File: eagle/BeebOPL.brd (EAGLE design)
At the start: 100 x 80 mm, 44 parts, among them IC1 LM324N, IC2 YM3014B, IC3 LM7805, IC5 74LS02N, IC6 YM3812, IC7 74LS04N, IC9 74HCT688N, J1 1 MHz Bus, J2 Feed-through, J3 3.5mm Jack, J4 DC-IN

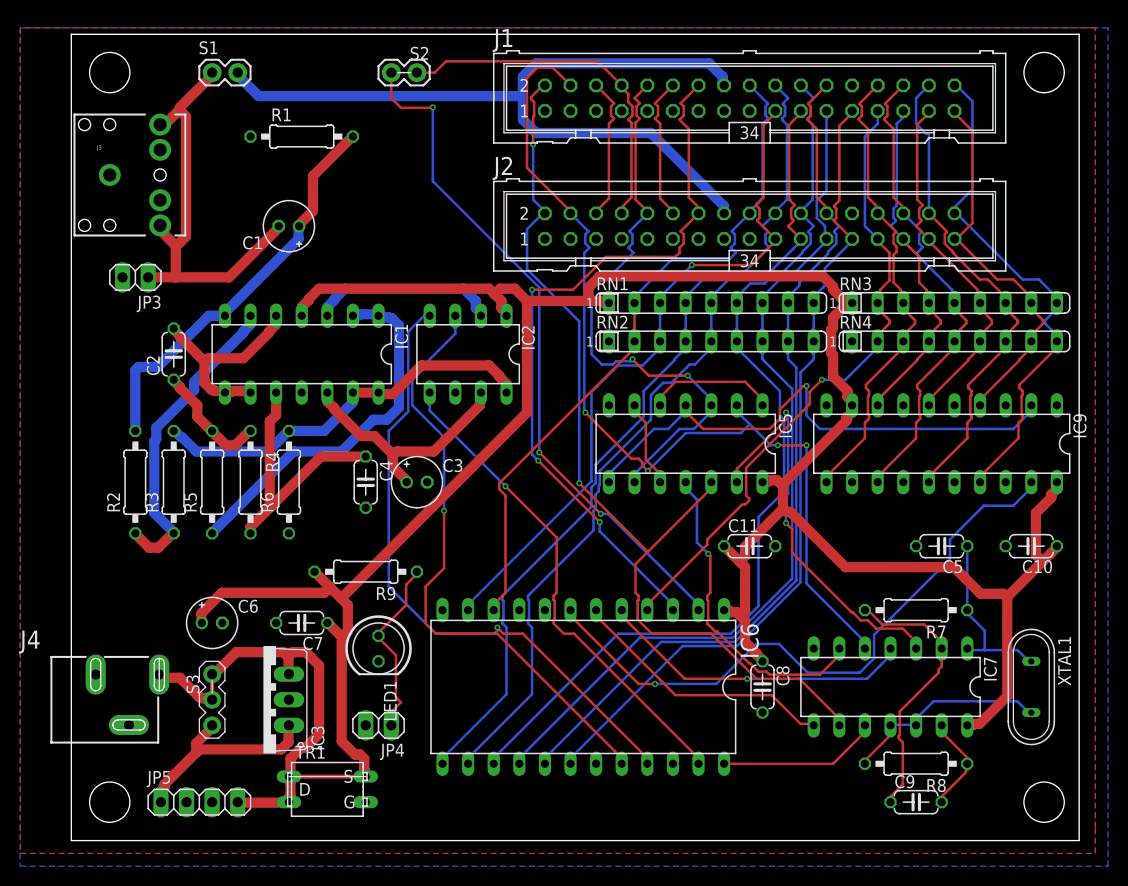
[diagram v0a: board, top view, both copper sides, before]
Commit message: Added silkscreen
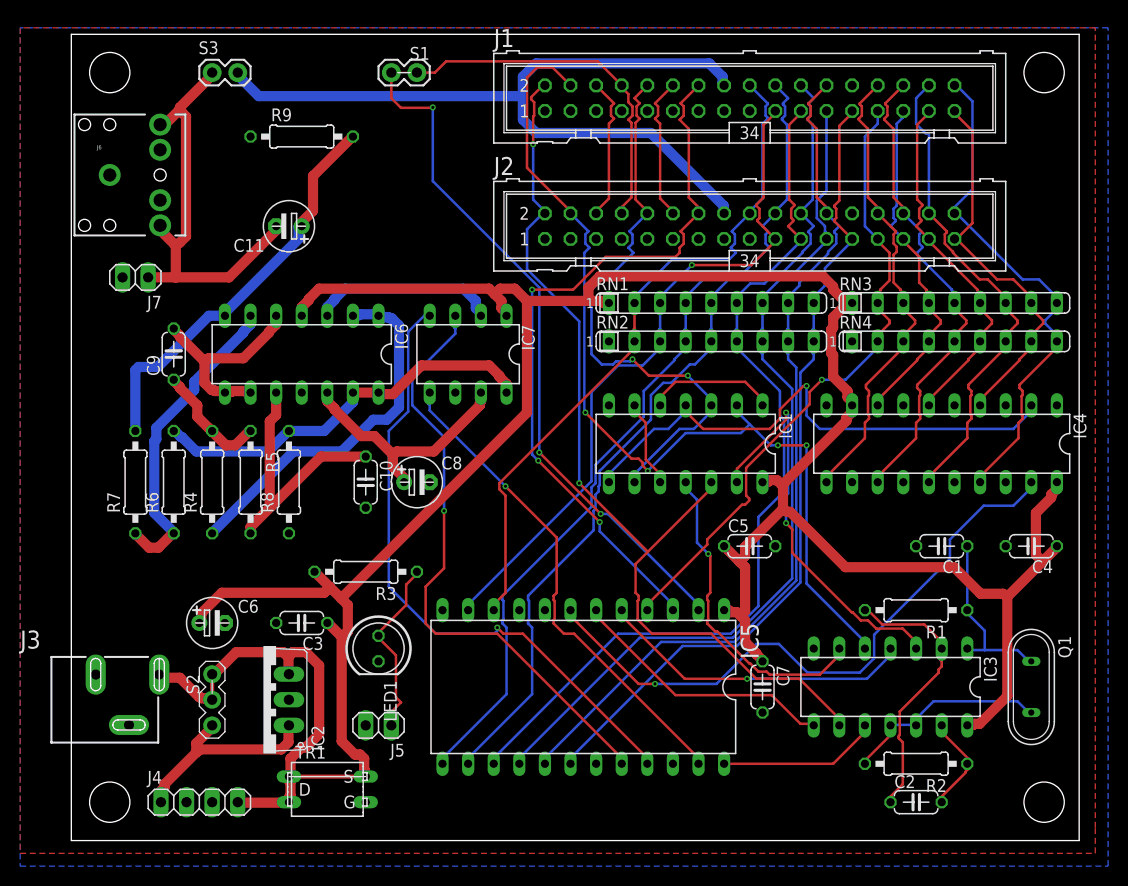
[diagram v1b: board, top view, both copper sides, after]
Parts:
- removed JP5: PWR, pinhead:1X04
- added J6: 3.5mm Jack, SparkFun-Connectors:AUDIO-JACK
- added LOGO1: OSHW-LOGO-BOTTOML, YMSynth:OSHW-LOGO-L
- C1: value 4.7uF 35V -> 82pF; device resistor:E2-5 -> resistor:C050-024X044
- C10: value 100nF -> 220pF
- C11: value 100nF -> 4.7uF 35V; device resistor:C050-024X044 -> YMSynth:E2,5-5
- C2: value 470pF -> 4.7nF
- C3: value 10uF 16V -> 10nF; device resistor:E2-5 -> resistor:C050-024X044
- C4: value 220pF -> 100nF
- C5: value 82pF -> 100nF
- C6: device resistor:E2-5 -> YMSynth:E2,5-5
- C8: value 10nF -> 10uF 16V; device resistor:C050-024X044 -> YMSynth:E2,5-5
- C9: value 4.7nF -> 470pF
- IC1: value LM324N -> 74LS02N; device linear:DIL14 -> 74xx-us:DIL14
- IC2: value YM3014B -> LM7805; device YMSynth:YM3014B -> linear:TO220V
- IC3: value LM7805 -> 74LS04N; device linear:TO220V -> 74xx-us:DIL14
- IC5: value 74LS02N -> YM3812; device 74xx-us:DIL14 -> YMSynth:YM3812
- IC6: value YM3812 -> LM324N; device YMSynth:YM3812 -> linear:DIL14
- IC7: value 74LS04N -> YM3014B; device 74xx-us:DIL14 -> YMSynth:YM3014B
- J3: value 3.5mm Jack -> DC in; device SparkFun-Connectors:AUDIO-JACK -> SparkFun-Connectors:POWER_JACK_SLOT
- J4: value DC-IN -> PWR; device SparkFun-Connectors:POWER_JACK_SLOT -> pinhead:1X04
- J7: value AUDIO -> Audio
- R1: value 4k7 -> 470R
- R2: value 27k -> 470R
- R3: value 15k -> 470R
- R6: value 4k7 -> 15k
- R7: value 470R -> 27k
- R8, R9: value 470R -> 4k7
- RN1, RN2, RN3, RN4: value 2k2 -> 2k2 x 8
- S1: value 1MHz Bus Audio -> IRQ enable; device SparkFun-Retired:1X02 -> YMSynth:1X02
- S2: value IRQ -> pwr sel; device YMSynth:1X02 -> YMSynth:S_3WAY_OR
- S3: value REG -> 1MHz Bus Audio; device YMSynth:S_3WAY_OR -> SparkFun-Retired:1X02
- moved C2 86.0 mm to (83.8, 3.81), turned to 0 degrees
- moved C9 86.0 mm to (10.2, 48.3), turned to 90 degrees
- moved R2 82.4 mm to (83.8, 7.62), turned to 180 degrees
- moved R7 78.5 mm to (6.35, 35.6), turned to 90 degrees
- moved R1 77.0 mm to (83.8, 22.9), turned to 180 degrees
- moved C1 72.1 mm to (86.4, 29.2)
- moved R8 68.2 mm to (21.6, 35.6), turned to 90 degrees
- moved C10 66.3 mm to (29.2, 35.6), turned to 270 degrees
- moved C4 66.3 mm to (95.2, 29.2), turned to 180 degrees
- moved S2 64.3 mm to (14.0, 15.2), turned to 270 degrees
- moved IC3 62.2 mm to (81.3, 15.2), turned to 180 degrees
- moved S3 61.0 mm to (14.0, 76.2), turned to 0 degrees
- moved C11 55.7 mm to (21.6, 61.0), turned to 180 degrees
- moved IC7 53.4 mm to (39.4, 48.3)
- moved J3 47.8 mm to (-5.08, 19.1), turned to 270 degrees
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- renumbered IC9 to IC4, JP3 to J7, JP4 to J5, XTAL1 to Q1
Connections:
- net +12V: now also IC2.1, J4.1, S2.3; no longer IC3.1, JP5.1, S3.3
- net +5V: now also IC2.3, J4.4, S2.1; no longer IC3.3, JP5.4, S3.1
- net /IRQ: now also S1.1; no longer S2.1
- net /PGFC: now also IC1.3, IC1.9; no longer IC5.3, IC5.9
- net /RST: now also IC5./IC; no longer IC6./IC
- net 1MHZE: now also IC1.2, IC3.5; no longer IC5.2, IC7.5
- net A0: now also IC5.A0; no longer IC6.A0
- net AUDIO: now also S3.2; no longer S1.2
- net AUDIO_OUT: now also C11.-, J6.RING, J6.TIP, S3.1; no longer C1.-, J3.RING, J3.TIP, S1.1
- net CNPGFC: now also IC1.4, IC1.8; no longer IC5.4, IC5.8
- net D0: now also IC5.D0; no longer IC6.D0
- net D1: now also IC5.D1; no longer IC6.D1
- net D2: now also IC5.D2; no longer IC6.D2
- net D3: now also IC5.D3; no longer IC6.D3
- net D4: now also IC5.D4; no longer IC6.D4
- net D5: now also IC5.D5; no longer IC6.D5
- net D6: now also IC5.D6; no longer IC6.D6
- net D7: now also IC5.D7; no longer IC6.D7
- net DC: now also J3.PWR, S2.2; no longer J4.PWR, S3.2
- net GND: now also C1.2, C3.2, C8.-, IC1.7, IC2.2, IC3.7, IC5.GND, IC6.11, IC7.GND, J3.GND@1, J3.GND@2, J4.2, J4.3, J6.SLEEVE, R8.1, R9.1; no longer C11.2, C3.-, C8.2, IC1.11, IC2.GND, IC3.2, IC5.7, IC6.GND, IC7.7, J3.SLEEVE, J4.GND@1, J4.GND@2, JP5.2, JP5.3, R1.1, R6.1
- net N$1: now also C2.1, IC3.2, R1.2; no longer C9.1, IC7.2, R7.2
- net N$10: now also IC1.1, IC1.5; no longer IC5.1, IC5.5
- net N$11: now also C8.+, IC6.12, IC7.RB; no longer C3.+, IC1.12, IC2.RB
- net N$12: now also IC1.10, IC1.6; no longer IC5.10, IC5.6
- net N$13: now also IC6.13, IC6.14, IC7.MP, R8.2; no longer IC1.13, IC1.14, IC2.MP, R3.2
- net N$14: now also IC3.8, IC5./RD; no longer IC6./RD, IC7.8
- net N$15: now also IC6.6, R6.1, R7.1; no longer IC1.6, R2.1, R3.1
- net N$16: now also C11.+, IC6.7, R7.2, R9.2; no longer C1.+, IC1.7, R1.2, R2.2
- net N$18: now also IC6.3, IC7.TOBUFF; no longer IC1.3, IC2.TOBUFF
- net N$19: now also IC6.1, IC6.2, R4.1; no longer IC1.1, IC1.2, R5.1
- net N$2: now also IC1.13, IC3.3; no longer IC5.13, IC7.3
- net N$20: now also C9.1, R4.2, R5.1; no longer C2.1, R4.1, R5.2
- net N$21: now also C10.1, IC6.10, R5.2; no longer C4.1, IC1.10, R4.2
- net N$22: now also C9.2, IC6.5, IC6.8, IC6.9; no longer C2.2, IC1.5, IC1.8, IC1.9
- net N$23: now also IC5./CS; no longer IC6./CS
- net N$24: now also IC3.4, IC5./WR; no longer IC6./WR, IC7.4
- net N$25: now also R3.1; no longer R9.1
- net N$26: now also IC3.10, IC5.0M; no longer IC6.0M, IC7.10
- net N$28: now also IC3.11, IC3.12, R2.2; no longer IC7.11, IC7.12, R8.2
- net N$3: now also IC1.11, IC3.6; no longer IC5.11, IC7.6
- net N$5: now also C2.2, IC3.13, R2.1; no longer C9.2, IC7.13, R8.1
- net N$6: now also IC5.SH, IC7.LOAD; no longer IC2.LOAD, IC6.SH
- net N$7: now also IC5.MO, IC7.SD; no longer IC2.SD, IC6.MO
- net N$8: now also IC5.0SY, IC7.CLOCK; no longer IC2.CLOCK, IC6.0SY
- net N$9: now also C1.1, IC3.1, R1.1; no longer C5.1, IC7.1, R7.1
- net R/W: now also IC1.12, IC3.9; no longer IC5.12, IC7.9
- net VCC: now also C3.1, C4.1, C5.1, IC1.14, IC3.14, IC5.VSS, IC6.4, IC7.VDD, R3.2; no longer C10.1, C11.1, C8.1, IC1.4, IC2.VDD, IC5.14, IC6.VSS, IC7.14, R9.2
- net YM/IRQ: now also IC5./IRQ, S1.2; no longer IC6./IRQ, S2.2
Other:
- board text added: "12V"
- board text added: "5V"
- board text added: "5V (12V)"
- board text added: "Bob's board"
- board text added: "GND"
- board text added: "Revision 1.00 Robert Lazarus 01.10.2016"
- board text added: "https://github.com/lazarusr/beebopl"

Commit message: Final board sent to fab
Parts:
- IC7: value YM3014B -> Y3014B
- moved LOGO1 14.7 mm to (68.5, 17.9)
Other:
- board text added: "BeebOPL Rev. 1.00 02.10.2016 Robert Lazarus https://github.com/lazarusr/beebopl"
- board text added: "Y3014B"
- board text added: "YM3812"
- board text removed: "Revision 1.00 Robert Lazarus 01.10.2016"
- board text removed: "https://github.com/lazarusr/beebopl"
